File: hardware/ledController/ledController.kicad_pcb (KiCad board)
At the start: 2 copper layers, 50 x 50 mm, 34 parts, among them IC1 PIC16F1769-I_ML, J1 Conn_01x06, J2 Screw_Terminal_01x02, J3 Screw_Terminal_01x02, J4 Conn_01x06, J5 Conn_01x02_Male, M1 LM2596_module, Q1 FMMT458TA, Q2 BUJ302AD

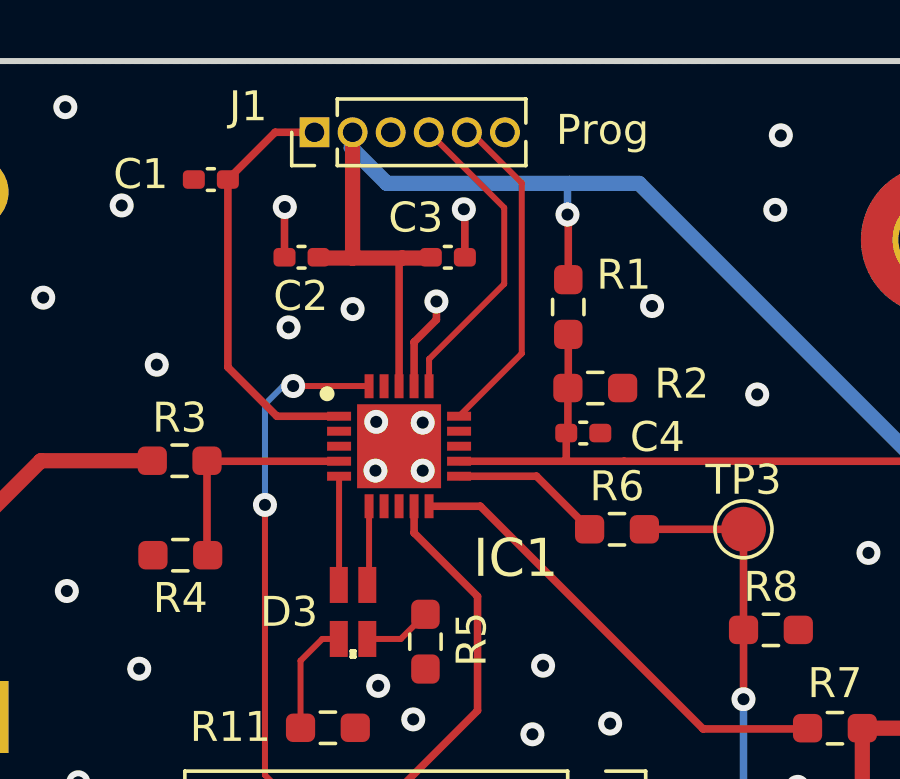
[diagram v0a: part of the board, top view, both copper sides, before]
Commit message: Version V1.1
Replaced PIC16F1769 with PIC16LF1709.  They are pin-to-pin
compatible with each other
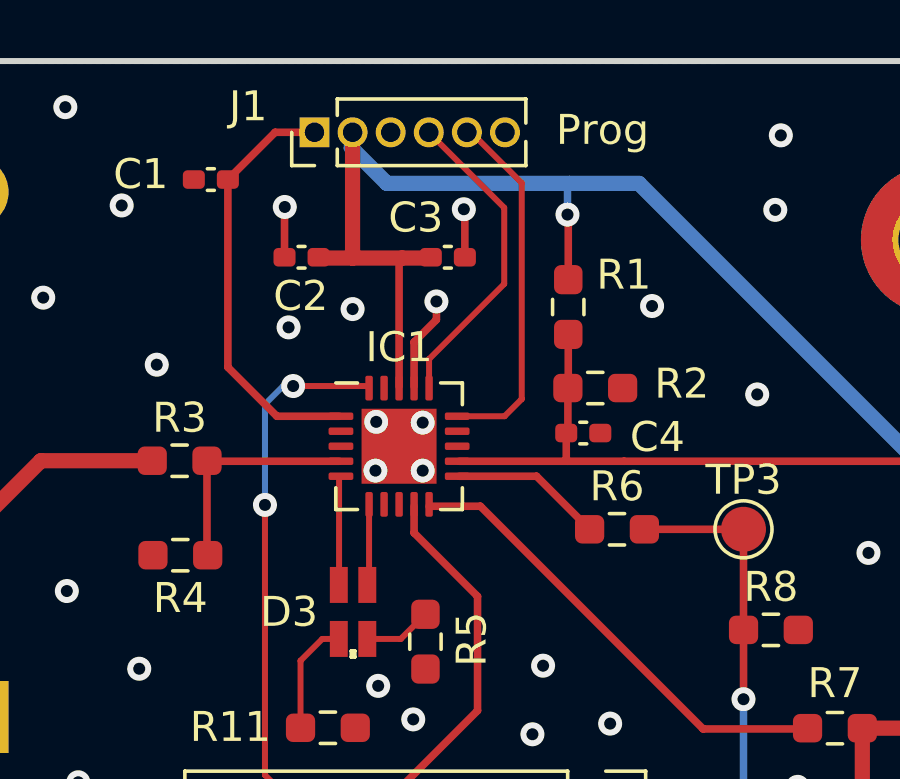
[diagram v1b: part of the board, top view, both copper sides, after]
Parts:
- IC1: value PIC16F1769-I_ML -> PIC16LF1709T-I_ML; footprint footprints:QFN50P400X400X100-21N-D -> Package_DFN_QFN:QFN-20-1EP_4x4mm_P0.5mm_EP2.5x2.5mm
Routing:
- net /PGC: track 11.2 -> 12.1 mm
